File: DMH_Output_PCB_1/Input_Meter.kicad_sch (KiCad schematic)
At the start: 29 parts, among them U21 TL072, U24 LM339, U25 LM339

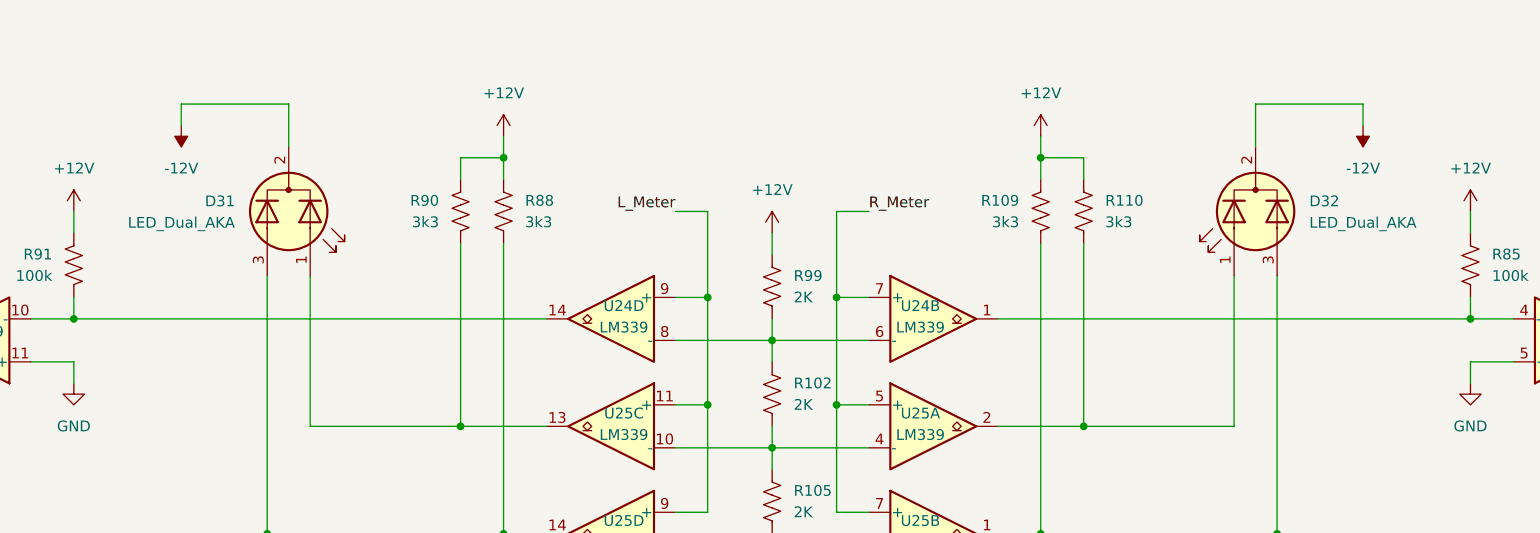
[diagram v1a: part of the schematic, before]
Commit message: Redesigned external input preamp
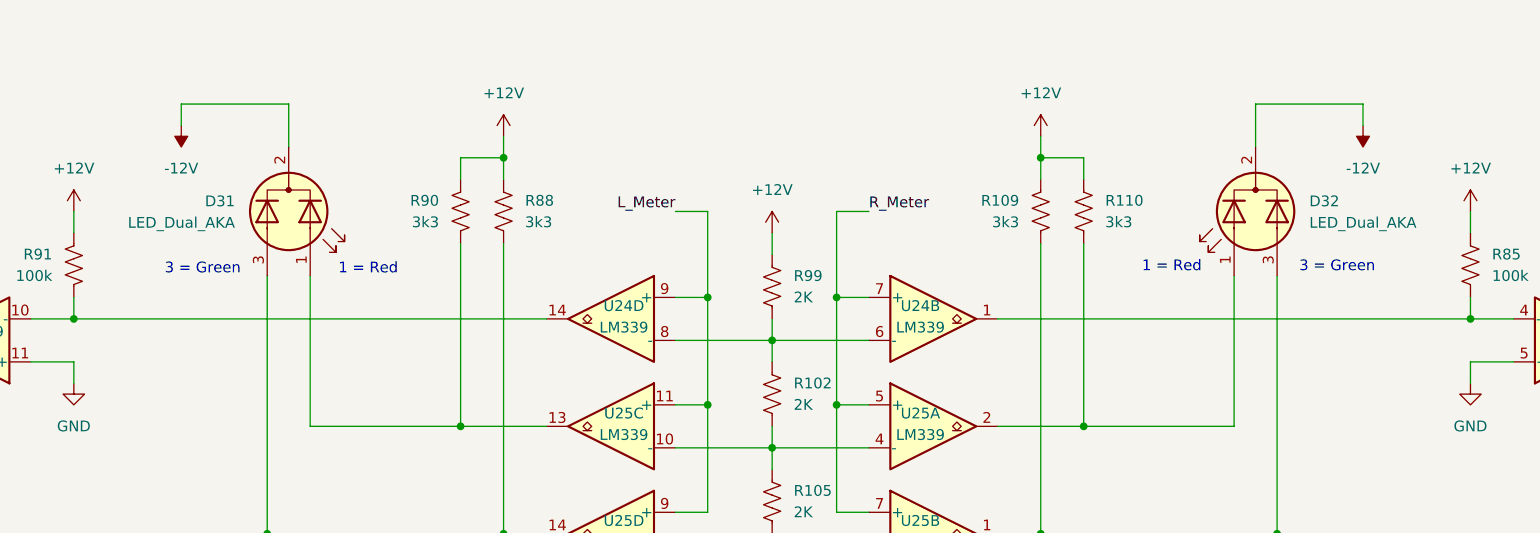
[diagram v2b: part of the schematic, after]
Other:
- note added: "1 = Red"
- note added: "3 = Green"
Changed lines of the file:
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@@
 		(comment 1 "PCB for 5 cm Kosmo format synthesizer module")
+	)
+	(text "3 = Green"
+		(exclude_from_sim no)
+		(at 91.44 121.158 0)
+		(effects
+			(font
+				(size 1.27 1.27)
+			)
+		)
+	)
+	(text "3 = Green"
+		(exclude_from_sim no)
+		(at 225.552 120.904 0)
+		(effects
+			(font
+				(size 1.27 1.27)
+			)
+		)
+	)
+	(text "1 = Red"
+		(exclude_from_sim no)
+		(at 110.998 121.158 0)
+		(effects
+			(font
+				(size 1.27 1.27)
+			)
+		)
+	)
+	(text "1 = Red"
+		(exclude_from_sim no)
+		(at 205.994 120.904 0)
+		(effects
+			(font
+				(size 1.27 1.27)
+			)
+		)
 	)
 	(junction

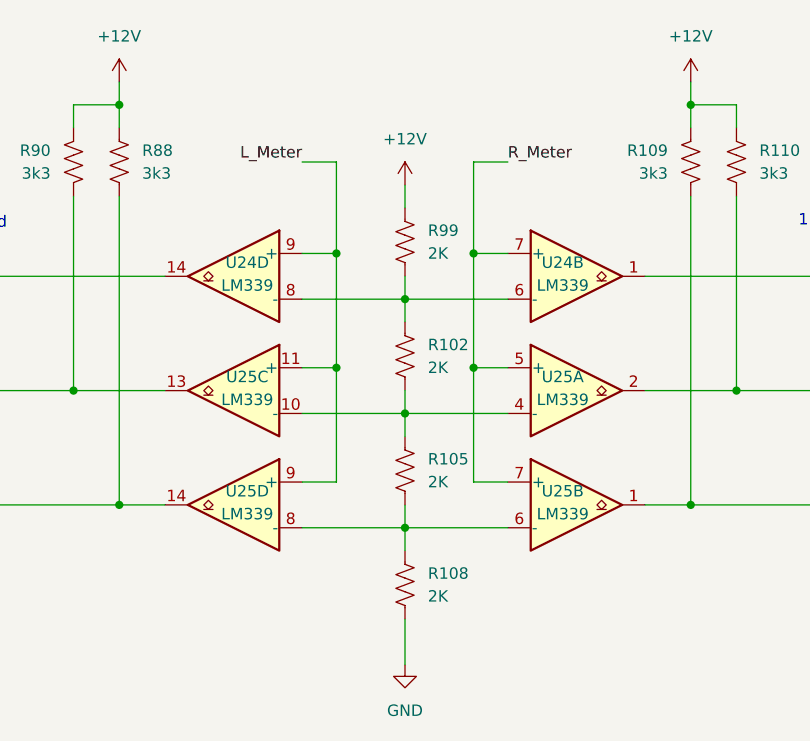
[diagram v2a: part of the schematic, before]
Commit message: Updated meters resistor values
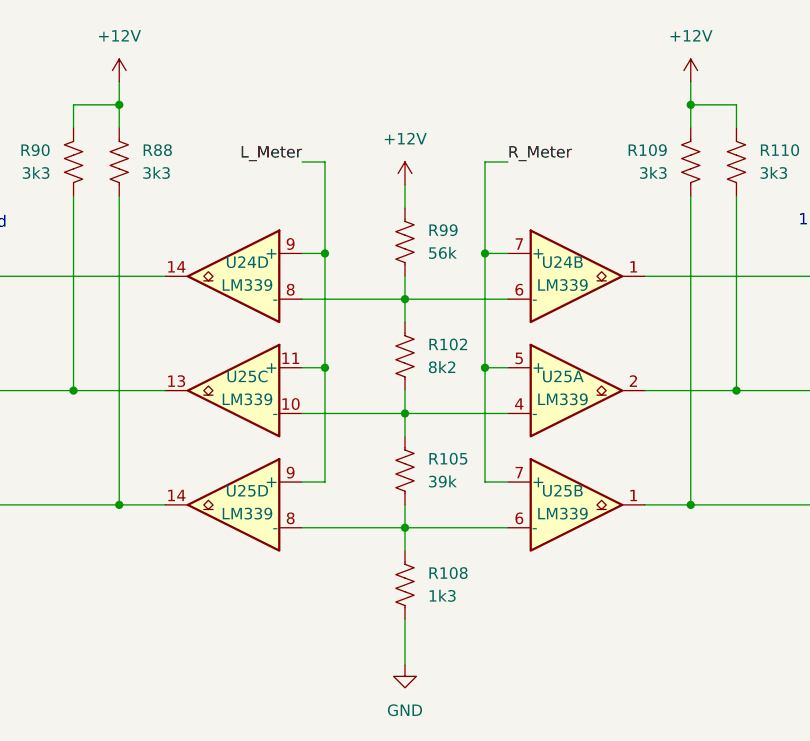
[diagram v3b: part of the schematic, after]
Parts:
- R102: value 2K -> 8k2
- R105: value 2K -> 39k
- R108: value 2K -> 1k3
- R99: value 2K -> 56k
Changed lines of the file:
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@@
 	)
 	(junction
-		(at 151.13 137.16)
+		(at 149.86 137.16)
 		(diameter 0)
 		(color 0 0 0 0)
@@
 	)
 	(junction
-		(at 166.37 124.46)
+		(at 167.64 124.46)
 		(diameter 0)
 		(color 0 0 0 0)
@@
 	)
 	(junction
-		(at 166.37 137.16)
+		(at 167.64 137.16)
 		(diameter 0)
 		(color 0 0 0 0)
@@
 	)
 	(junction
-		(at 151.13 124.46)
+		(at 149.86 124.46)
 		(diameter 0)
 		(color 0 0 0 0)
@@
 	(wire
 		(pts
-			(xy 166.37 124.46) (xy 166.37 137.16)
+			(xy 167.64 124.46) (xy 167.64 137.16)
 		)
 		(stroke
@@
 	(wire
 		(pts
-			(xy 151.13 124.46) (xy 151.13 137.16)
+			(xy 149.86 124.46) (xy 149.86 137.16)
 		)
 		(stroke
@@
 	(wire
 		(pts
-			(xy 166.37 137.16) (xy 170.18 137.16)
+			(xy 167.64 137.16) (xy 170.18 137.16)
 		)
 		(stroke
@@
 	(wire
 		(pts
-			(xy 166.37 124.46) (xy 170.18 124.46)
+			(xy 167.64 124.46) (xy 170.18 124.46)
 		)
 		(stroke
@@
 	(wire
 		(pts
-			(xy 151.13 137.16) (xy 151.13 149.86)
+			(xy 149.86 137.16) (xy 149.86 149.86)
 		)
 		(stroke
@@
 	(wire
 		(pts
-			(xy 170.18 114.3) (xy 166.37 114.3)
+			(xy 170.18 114.3) (xy 167.64 114.3)
 		)
 		(stroke
@@
 	(wire
 		(pts
-			(xy 151.13 149.86) (xy 147.32 149.86)
+			(xy 149.86 149.86) (xy 147.32 149.86)
 		)
 		(stroke
@@
 	(wire
 		(pts
-			(xy 166.37 149.86) (xy 170.18 149.86)
+			(xy 167.64 149.86) (xy 170.18 149.86)
 		)
 		(stroke
@@
 	(wire
 		(pts
-			(xy 151.13 114.3) (xy 151.13 124.46)
+			(xy 149.86 114.3) (xy 149.86 124.46)
 		)
 		(stroke
@@
 	(wire
 		(pts
-			(xy 166.37 137.16) (xy 166.37 149.86)
+			(xy 167.64 137.16) (xy 167.64 149.86)
 		)
 		(stroke
@@
 	(wire
 		(pts
-			(xy 147.32 137.16) (xy 151.13 137.16)
+			(xy 147.32 137.16) (xy 149.86 137.16)
 		)
 		(stroke
@@
 	(wire
 		(pts
-			(xy 147.32 114.3) (xy 151.13 114.3)
+			(xy 147.32 114.3) (xy 149.86 114.3)
 		)
 		(stroke
@@
 	(wire
 		(pts
-			(xy 166.37 114.3) (xy 166.37 124.46)
+			(xy 167.64 114.3) (xy 167.64 124.46)
 		)
 		(stroke
@@
 	(wire
 		(pts
-			(xy 147.32 124.46) (xy 151.13 124.46)
+			(xy 147.32 124.46) (xy 149.86 124.46)
 		)
 		(stroke
@@
 			)
 		)
-		(property "Value" "2K"
+		(property "Value" "8k2"
 			(at 161.29 137.1599 0)
 			(effects
@@
 			)
 		)
-		(property "Value" "2K"
+		(property "Value" "39k"
 			(at 161.29 149.8599 0)
 			(effects
@@
 			)
 		)
-		(property "Value" "2K"
+		(property "Value" "56k"
 			(at 161.29 124.4599 0)
 			(effects
@@
 			)
 		)
-		(property "Value" "2K"
+		(property "Value" "1k3"
 			(at 161.29 162.5599 0)
 			(effects

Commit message: Adjustments during breadboarding
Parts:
- removed U21: TL072, Package_DIP:DIP-8_W7.62mm_Socket, symbol Amplifier_Operational:TL072
- added U20: TL072, Package_DIP:DIP-8_W7.62mm_Socket, symbol Amplifier_Operational:TL072
- R89, R97: value 20K -> 20k
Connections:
- net GND: now also U20.3 (+), U20.5 (+)
- net at D33.1 (K), D34.2 (A): now also U20.1
- net at D33.2 (A), R84.1, R89.2: now also U20.2 (-)
- net at D43.2 (A), R92.1, R97.2: now also U20.6 (-)
- net at D43.1 (K), D44.2 (A): now also U20.7
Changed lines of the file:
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@@
 	)
 	(symbol
-		(lib_id "Amplifier_Operational:TL072")
-		(at 50.8 50.8 0)
-		(mirror x)
-		(unit 1)
-		(exclude_from_sim no)
-		(in_bom yes)
-		(on_board yes)
-		(dnp no)
-		(property "Reference" "U21"
-			(at 50.8 60.96 0)
-			(effects
-				(font
-					(size 1.27 1.27)
-				)
-			)
-		)
-		(property "Value" "TL072"
-			(at 50.8 58.42 0)
-			(effects
-				(font
-					(size 1.27 1.27)
-				)
-			)
-		)
-		(property "Footprint" "Package_DIP:DIP-8_W7.62mm_Socket"
-			(at 50.8 50.8 0)
-			(effects
-				(font
-					(size 1.27 1.27)
-				)
-				(hide yes)
-			)
-		)
-		(property "Datasheet" "http://www.ti.com/lit/ds/symlink/tl071.pdf"
-			(at 50.8 50.8 0)
-			(effects
-				(font
-					(size 1.27 1.27)
-				)
-				(hide yes)
-			)
-		)
-		(property "Description" "Dual Low-Noise JFET-Input Operational Amplifiers, DIP-8/SOIC-8"
-			(at 50.8 50.8 0)
-			(effects
-				(font
-					(size 1.27 1.27)
-				)
-				(hide yes)
-			)
-		)
-		(property "Function" ""
-			(at 50.8 50.8 0)
-			(effects
-				(font
-					(size 1.27 1.27)
-				)
-			)
-		)
-		(pin "5"
-		)
-		(pin "2"
-		)
-		(pin "4"
-		)
-		(pin "3"
-		)
-		(pin "1"
-		)
-		(pin "6"
-		)
-		(pin "7"
-		)
-		(pin "8"
-		)
-		(instances
-			(project "DMH_Output_PCB_1"
-				(path "/58f4306d-5387-4983-bb08-41a2313fd315/55c0022e-9ebc-4247-b070-6524df6af06d"
-					(reference "U21")
-					(unit 1)
-				)
-			)
-		)
-	)
-	(symbol
 		(lib_id "Device:R_US")
 		(at 121.92 114.3 0)
@@
 	)
 	(symbol
-		(lib_id "Amplifier_Operational:TL072")
-		(at 165.1 50.8 0)
-		(mirror x)
-		(unit 2)
-		(exclude_from_sim no)
-		(in_bom yes)
-		(on_board yes)
-		(dnp no)
-		(property "Reference" "U21"
-			(at 165.1 60.96 0)
-			(effects
-				(font
-					(size 1.27 1.27)
-				)
-			)
-		)
-		(property "Value" "TL072"
-			(at 165.1 58.42 0)
-			(effects
-				(font
-					(size 1.27 1.27)
-				)
-			)
-		)
-		(property "Footprint" "Package_DIP:DIP-8_W7.62mm_Socket"
-			(at 165.1 50.8 0)
-			(effects
-				(font
-					(size 1.27 1.27)
-				)
-				(hide yes)
-			)
-		)
-		(property "Datasheet" "http://www.ti.com/lit/ds/symlink/tl071.pdf"
-			(at 165.1 50.8 0)
-			(effects
-				(font
-					(size 1.27 1.27)
-				)
-				(hide yes)
-			)
-		)
-		(property "Description" "Dual Low-Noise JFET-Input Operational Amplifiers, DIP-8/SOIC-8"
-			(at 165.1 50.8 0)
-			(effects
-				(font
-					(size 1.27 1.27)
-				)
-				(hide yes)
-			)
-		)
-		(property "Function" ""
-			(at 165.1 50.8 0)
-			(effects
-				(font
-					(size 1.27 1.27)
-				)
-			)
-		)
-		(pin "5"
-		)
-		(pin "2"
-		)
-		(pin "4"
-		)
-		(pin "3"
-		)
-		(pin "1"
-		)
-		(pin "6"
-		)
-		(pin "7"
-		)
-		(pin "8"
-		)
-		(instances
-			(project "DMH_Output_PCB_1"
-				(path "/58f4306d-5387-4983-bb08-41a2313fd315/55c0022e-9ebc-4247-b070-6524df6af06d"
-					(reference "U21")
-					(unit 2)
-				)
-			)
-		)
-	)
-	(symbol
 		(lib_id "Device:R_US")
 		(at 215.9 44.45 180)
@@
 			)
 		)
-		(property "Value" "20K"
+		(property "Value" "20k"
 			(at 146.05 44.45 90)
 			(effects
@@
 			)
 		)
-		(property "Value" "20K"
+		(property "Value" "20k"
 			(at 31.75 44.45 90)
 			(effects
@@
 	)
 	(symbol
+		(lib_id "Amplifier_Operational:TL072")
+		(at 50.8 50.8 0)
+		(mirror x)
+		(unit 1)
+		(exclude_from_sim no)
+		(in_bom yes)
+		(on_board yes)
+		(dnp no)
+		(property "Reference" "U20"
+			(at 50.8 60.96 0)
+			(effects
+				(font
+					(size 1.27 1.27)
+				)
+			)
+		)
+		(property "Value" "TL072"
+			(at 50.8 58.42 0)
+			(effects
+				(font
+					(size 1.27 1.27)
+				)
+			)
+		)
+		(property "Footprint" "Package_DIP:DIP-8_W7.62mm_Socket"
+			(at 50.8 50.8 0)
+			(effects
+				(font
+					(size 1.27 1.27)
+				)
+				(hide yes)
+			)
+		)
+		(property "Datasheet" "http://www.ti.com/lit/ds/symlink/tl071.pdf"
+			(at 50.8 50.8 0)
+			(effects
+				(font
+					(size 1.27 1.27)
+				)
+				(hide yes)
+			)
+		)
+		(property "Description" "Dual Low-Noise JFET-Input Operational Amplifiers, DIP-8/SOIC-8"
+			(at 50.8 50.8 0)
+			(effects
+				(font
+					(size 1.27 1.27)
+				)
+				(hide yes)
+			)
+		)
+		(pin "7"
+		)
+		(pin "2"
+		)
+		(pin "6"
+		)
+		(pin "3"
+		)
+		(pin "8"
+		)
+		(pin "4"
+		)
+		(pin "1"
+		)
+		(pin "5"
+		)
+		(instances
+			(project "DMH_Output_PCB_1"
+				(path "/58f4306d-5387-4983-bb08-41a2313fd315/55c0022e-9ebc-4247-b070-6524df6af06d"
+					(reference "U20")
+					(unit 1)
+				)
+			)
+		)
+	)
+	(symbol
 		(lib_id "Device:R_US")
 		(at 82.55 38.1 90)
@@
 				)
 			)
+		)
+	)
+	(symbol
+		(lib_id "Amplifier_Operational:TL072")
+		(at 165.1 50.8 0)
+		(mirror x)
+		(unit 2)
+		(exclude_from_sim no)
+		(in_bom yes)
+		(on_board yes)
+		(dnp no)
+		(property "Reference" "U20"
+			(at 165.1 60.96 0)
+			(effects
+				(font
+					(size 1.27 1.27)
+				)
+			)
+		)
+		(property "Value" "TL072"
+			(at 165.1 58.42 0)
+			(effects
+				(font
+					(size 1.27 1.27)
+				)
+			)
+		)
+		(property "Footprint" "Package_DIP:DIP-8_W7.62mm_Socket"
+			(at 165.1 50.8 0)
+			(effects
+				(font
+					(size 1.27 1.27)
+				)
+				(hide yes)
+			)
+		)
+		(property "Datasheet" "http://www.ti.com/lit/ds/symlink/tl071.pdf"
+			(at 165.1 50.8 0)
+			(effects
+				(font
+					(size 1.27 1.27)
+				)
+				(hide yes)
+			)
+		)
+		(property "Description" "Dual Low-Noise JFET-Input Operational Amplifiers, DIP-8/SOIC-8"
+			(at 165.1 50.8 0)
+			(effects
+				(font
+					(size 1.27 1.27)
+				)
+				(hide yes)
+			)
+		)
+		(pin "7"
+		)
+		(pin "2"
+		)
+		(pin "6"
+		)
+		(pin "3"
+		)
+		(pin "8"
+		)
+		(pin "4"
+		)
+		(pin "1"
+		)
+		(pin "5"
+		)
+		(instances
+			(project "DMH_Output_PCB_1"
+				(path "/58f4306d-5387-4983-bb08-41a2313fd315/55c0022e-9ebc-4247-b070-6524df6af06d"
+					(reference "U20")
+					(unit 2)
+				)
+			)
